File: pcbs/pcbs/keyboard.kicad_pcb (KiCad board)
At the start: 2 copper layers, 152.4 x 110.9 mm, 96 parts, among them J1 Jumper, J10 Jumper, J11 Jumper, J12 Jumper, J13 Jumper, J14 Jumper, J15 Jumper, J16 Jumper, J17 Jumper, J18 Jumper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

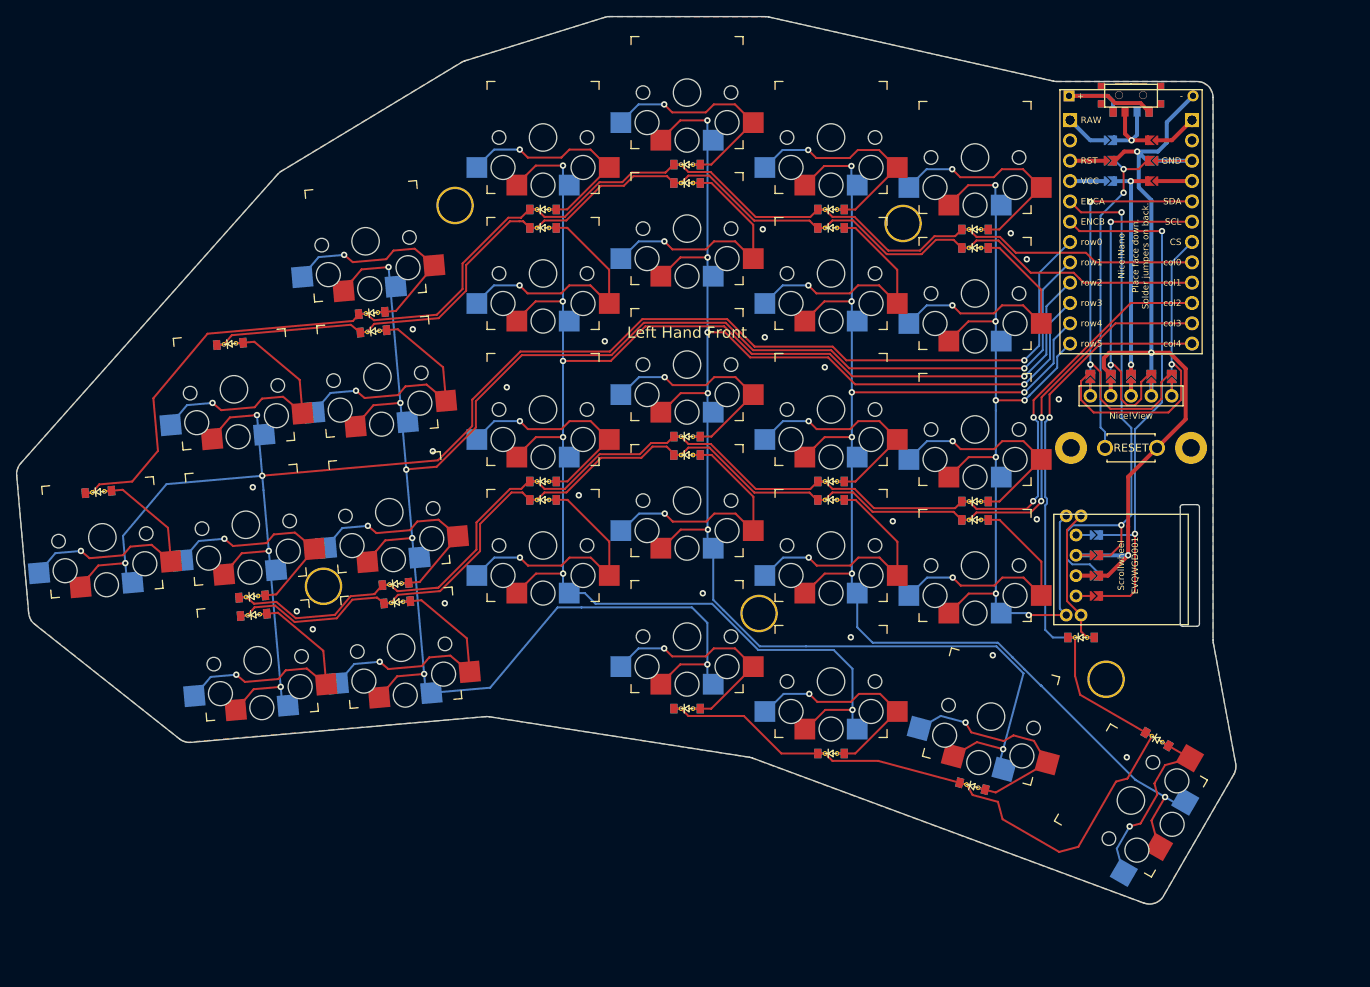
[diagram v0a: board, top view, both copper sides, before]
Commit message: Squashed commit of the following:
commit bb18cddcc8a03dbf4a5a163c8480892c78f4e76d
Author: daniel <github@dbauer.me>
Date:   Sat Aug 5 11:43:33 2023 +0200

    update gerbers

commit df5ee882de9ff45955de45abaf159e16f07e81d5
Author: daniel <github@dbauer.me>
Date:   Sat Aug 5 11:43:15 2023 +0200

    pcb render

commit 14c23b0fa81e10e23a27a0ec447a32f917531800
Author: daniel <github@dbauer.me>
Date:   Sat Aug 5 11:34:24 2023 +0200

    add icon svg

commit 6ec17faa04a79be8401f3ef865241375cf1b13ce
Author: daniel <github@dbauer.me>
Date:   Sat Aug 5 11:31:08 2023 +0200

    Update README.md

commit b65a183fe34a89897199075e95691768964b1521
Author: daniel <github@dbauer.me>
Date:   Sat Aug 5 11:30:20 2023 +0200

    routed rev 1.1

commit 9ce5d4ee41848c9c1b13896db0a7d9f578373969
Author: daniel <github@dbauer.me>
Date:   Sat Aug 5 09:46:20 2023 +0200

    add rev and order number to ergogen config

commit c0575a7352caa34b94f202d832875772e4f1c2db
Author: daniel <github@dbauer.me>
Date:   Sat Aug 5 08:56:18 2023 +0200

    make text on pcb better readable

commit 03692059b53d9f7ae5ba01feed3b92d08a4c8239
Author: daniel <github@dbauer.me>
Date:   Sat Aug 5 08:44:04 2023 +0200

    fix mcu labels

commit 6edd65c0c5cc4938772bcfffd58f7a8371476361
Author: daniel <github@dbauer.me>
Date:   Sat Aug 5 08:34:36 2023 +0200

    incr. diode to socket distance
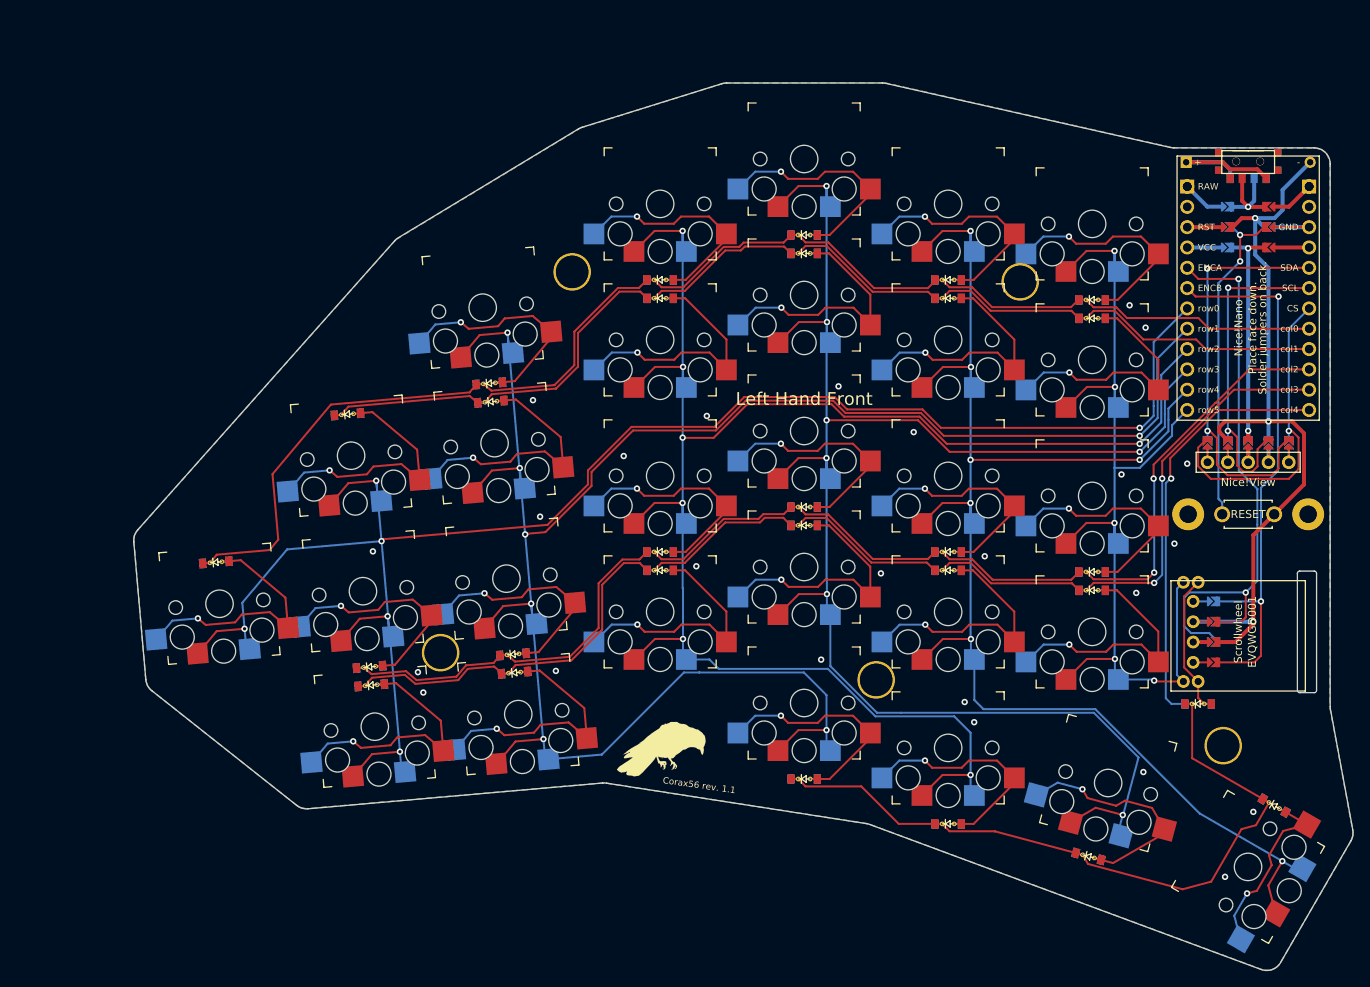
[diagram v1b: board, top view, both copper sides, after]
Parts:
- removed the ? at (117.3, 67.4) (x2)
- removed the S20 at (135.3, 77.0)
- removed the S20 at (153.3, 79.5)
- added ? (x2): , lib:text, F.Cu at (122.9, 124.7)
- added ? (x2): , lib:text, F.Cu at (131.9, 75.7)
- added ?: , lib:text, F.Cu at (174.0, 137.4)
- added S20: , PG1350, F.Cu at (149.9, 85.3)
- added S24: , PG1350, F.Cu at (167.9, 87.8)
- moved D3 17.1 mm to (92.6, 73.8)
- moved D2 17.1 mm to (95.5, 107.6)
- moved D17 17.1 mm to (74.8, 77.6)
- moved D16 17.1 mm to (77.8, 111.5)
- moved D1 17.1 mm to (77.6, 109.2)
- moved D19 17.1 mm to (92.8, 76.1)
- moved D18 17.1 mm to (95.7, 109.9)
- moved D15 17.1 mm to (58.4, 96.1)
- moved D11 17.1 mm to (149.9, 60.8)
- moved D13 17.1 mm to (167.9, 63.3)
- moved D25 17.1 mm to (149.9, 63.1)
- moved D6 17.1 mm to (131.9, 123.2)
- moved D20 17.1 mm to (113.9, 97.1)
- moved D12 17.1 mm to (167.9, 97.3)
- moved D7 17.1 mm to (131.9, 89.2)
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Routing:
- net row5: track 117.3 -> 124.7 mm, vias 7 -> 5
- net row4: track 176.5 -> 183.9 mm
- net row2: track 213.1 -> 220.3 mm
- net col4: track 150.9 -> 145.8 mm
- net row1: track 242.4 -> 247.5 mm
- net row3: track 206.2 -> 211.2 mm
- net row0: track 215.9 -> 219.1 mm
- net ENCA: track 68.3 -> 71.2 mm
- net GND: track 92.3 -> 94.1 mm, vias 24 -> 28
- net ENCB: track 67.2 -> 68.7 mm
- net col3: track 160.9 -> 162.2 mm
- net col1: track 148.0 -> 146.7 mm
- net RST: track 41.9 -> 41.0 mm
- net col2: track 161.9 -> 162.7 mm
- net inner_bottom: track 34.0 -> 33.4 mm
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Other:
- board text removed: "JLCJLCJLCJLC"
